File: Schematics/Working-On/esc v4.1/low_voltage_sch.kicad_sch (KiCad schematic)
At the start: 28 parts, among them IC1 74HCT08BQ,115, IC2 74HCT08BQ,115, U2 ATmega328P-M

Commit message: New connectors, and BEMF Filter.
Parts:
- removed C12: 8200pF, Capacitor_SMD:C_0402_1005Metric, symbol Device:C
- added C24: 2.5n, Capacitor_SMD:C_0402_1005Metric, symbol Device:C
- added R23, R24, R5: 10k, Resistor_SMD:R_0402_1005Metric, symbol Device:R
- 8MHz1: value ECS-80-12-30BQ-JES-TR -> ECS-80-12-33-JGN-TR; footprint ECS-80-12-30BQ-JES-TR:ECS-80-12_ECS -> Crystal:Crystal_SMD_3225-4Pin_3.2x2.5mm
- C11, C7: value 8200pF -> 2.5n
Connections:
- net COIL_A_BEMF: now also C7.2, R5.2; no longer C7.1, R3.1, R4.2
- net COIL_B_BEMF: now also C11.2, R23.2; no longer C11.1, R6.1, R7.2
- net COIL_C_BEMF: now also C24.2, R24.2; no longer R19.1, R20.2
- net GND: now also C11.1, C7.1, C24.1; no longer C11.2, C7.2
- net PWM: now reaches U2.1 (PD3)
- new net: R19.1, R20.2, R24.1
- new net: R23.1, R6.1, R7.2
- new net: R3.1, R4.2, R5.1
- no-connect marks 11 -> 10
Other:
- moved on the sheet: C11, C13, C19, C7, IC1, IC2, R19, R20, R3, R4, R6, R7

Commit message: VIA update
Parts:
- removed R9: 1k, Resistor_SMD:R_0402_1005Metric, symbol Device:R
- added C12: 47uF, Capacitor_SMD:C_0805_2012Metric, symbol Device:C
- added L2: 100uH, Inductor_SMD:L_0805_2012Metric, symbol Device:L
- C11, C24, C7: value 2.5n -> 2.4n
- C23: value 10uF -> 47uF; footprint Capacitor_SMD:C_0603_1608Metric -> Capacitor_SMD:C_0805_2012Metric
- L1: value 2.2mH -> 100uH; footprint 744045222:WE-LQ_L49 -> Inductor_SMD:L_0805_2012Metric
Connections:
- net COMP_REF_IN: now also C12.2, L2.2; no longer C23.2, L1.2
- net GND: now also C12.1
- new net: C23.2, L1.2, L2.1
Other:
- note removed: "fc = 1 kHz"
- moved on the sheet: C23, L1, R1, R8

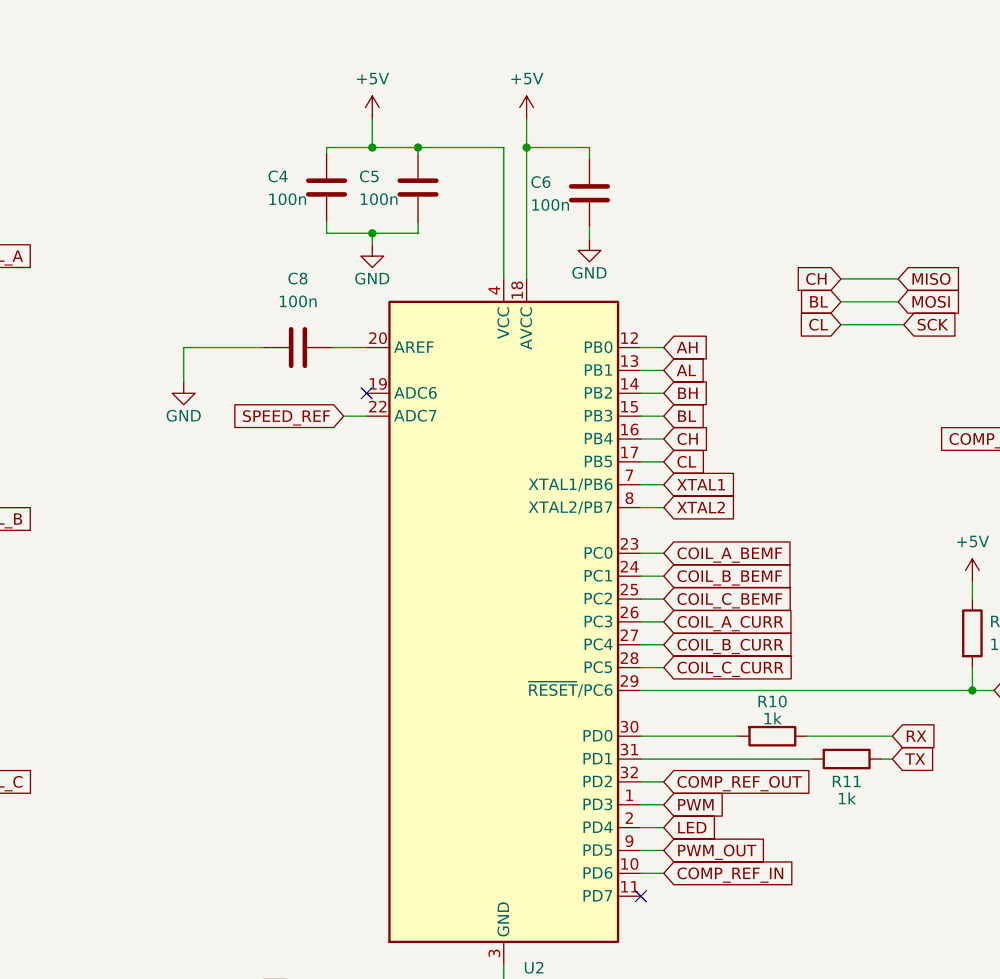
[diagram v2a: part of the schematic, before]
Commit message: swaped PWM_IN & Comp_Ref_Out, vias finished
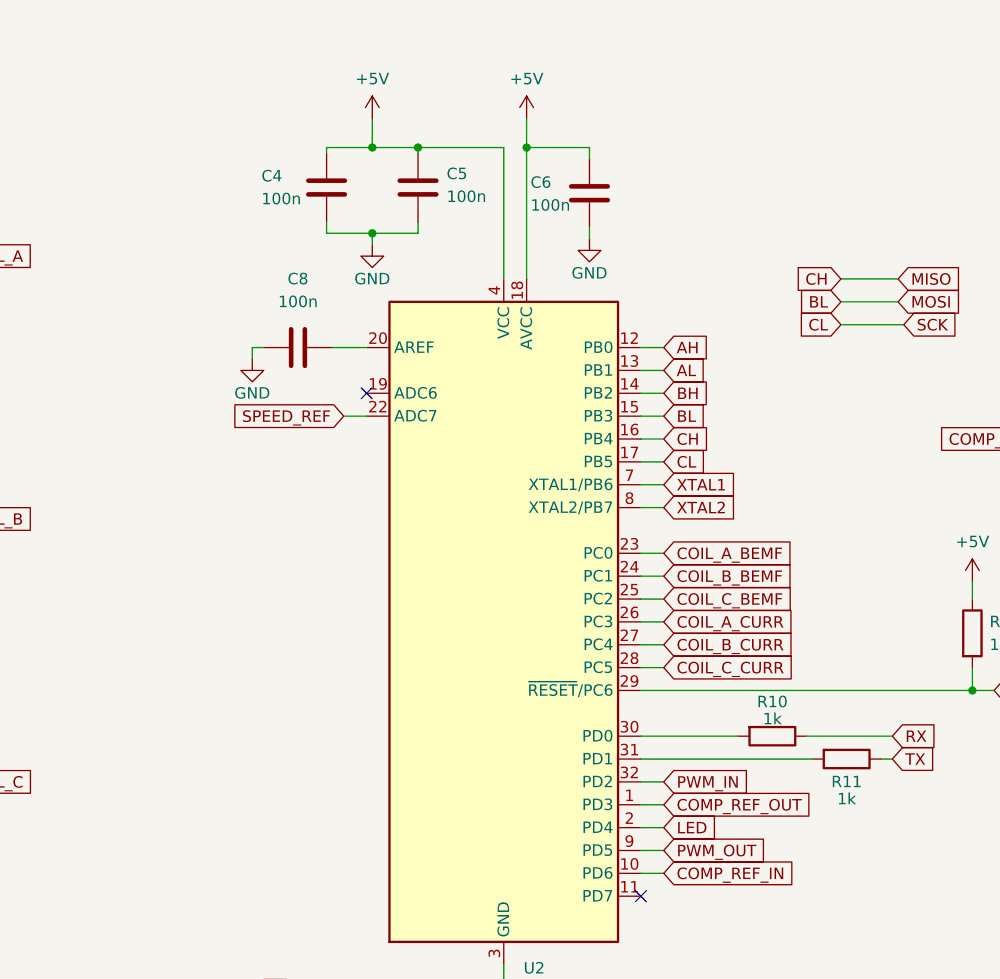
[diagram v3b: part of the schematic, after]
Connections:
- net PWM is gone; now on net COMP_REF_OUT: U2.1 (PD3)
- net COMP_REF_OUT: no longer U2.32 (PD2)
- new net PWM_IN: U2.32 (PD2)
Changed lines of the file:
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@@
 	(wire
 		(pts
-			(xy 120.65 71.12) (xy 120.65 74.93)
+			(xy 128.27 71.12) (xy 128.27 72.39)
 		)
 		(stroke
@@
 	(wire
 		(pts
-			(xy 129.54 71.12) (xy 120.65 71.12)
+			(xy 128.27 71.12) (xy 129.54 71.12)
 		)
 		(stroke
@@
 		)
 	)
-	(global_label "PWM"
+	(global_label "PWM_IN"
 		(shape input)
-		(at 173.99 121.92 0)
+		(at 173.99 119.38 0)
 		(fields_autoplaced yes)
 		(effects
@@
 		)
 		(property "Intersheetrefs" "${INTERSHEET_REFS}"
-			(at 181.148 121.92 0)
+			(at 184.0509 119.38 0)
 			(effects
 				(font
@@
 	(global_label "COMP_REF_OUT"
 		(shape input)
-		(at 173.99 119.38 0)
+		(at 173.99 121.92 0)
 		(fields_autoplaced yes)
 		(effects
@@
 		)
 		(property "Intersheetrefs" "${INTERSHEET_REFS}"
-			(at 191.3685 119.38 0)
+			(at 191.3685 121.92 0)
 			(effects
 				(font
@@
 		(dnp no)
 		(property "Reference" "C5"
-			(at 140.1318 52.1462 0)
+			(at 149.86 51.816 0)
 			(effects
 				(font
@@
 		)
 		(property "Value" "100n"
-			(at 140.1318 54.6862 0)
+			(at 149.86 54.356 0)
 			(effects
 				(font
@@
 		(dnp no)
 		(property "Reference" "C4"
-			(at 129.9718 52.1462 0)
+			(at 129.286 52.07 0)
 			(effects
 				(font
@@
 		)
 		(property "Value" "100n"
-			(at 129.9718 54.6862 0)
+			(at 129.286 54.61 0)
 			(effects
 				(font
@@
 	(symbol
 		(lib_id "power:GND")
-		(at 120.65 74.93 0)
+		(at 128.27 72.39 0)
 		(unit 1)
 		(exclude_from_sim no)
@@
 		(dnp no)
 		(property "Reference" "#PWR019"
-			(at 120.65 81.28 0)
+			(at 128.27 78.74 0)
 			(effects
 				(font
@@
 		)
 		(property "Value" "GND"
-			(at 120.65 78.74 0)
+			(at 128.27 76.2 0)
 			(effects
 				(font
@@
 		)
 		(property "Footprint" ""
-			(at 120.65 74.93 0)
+			(at 128.27 72.39 0)
 			(effects
 				(font
@@
 		)
 		(property "Datasheet" ""
-			(at 120.65 74.93 0)
+			(at 128.27 72.39 0)
 			(effects
 				(font
@@
 		)
 		(property "Description" ""
-			(at 120.65 74.93 0)
+			(at 128.27 72.39 0)
 			(effects
 				(font

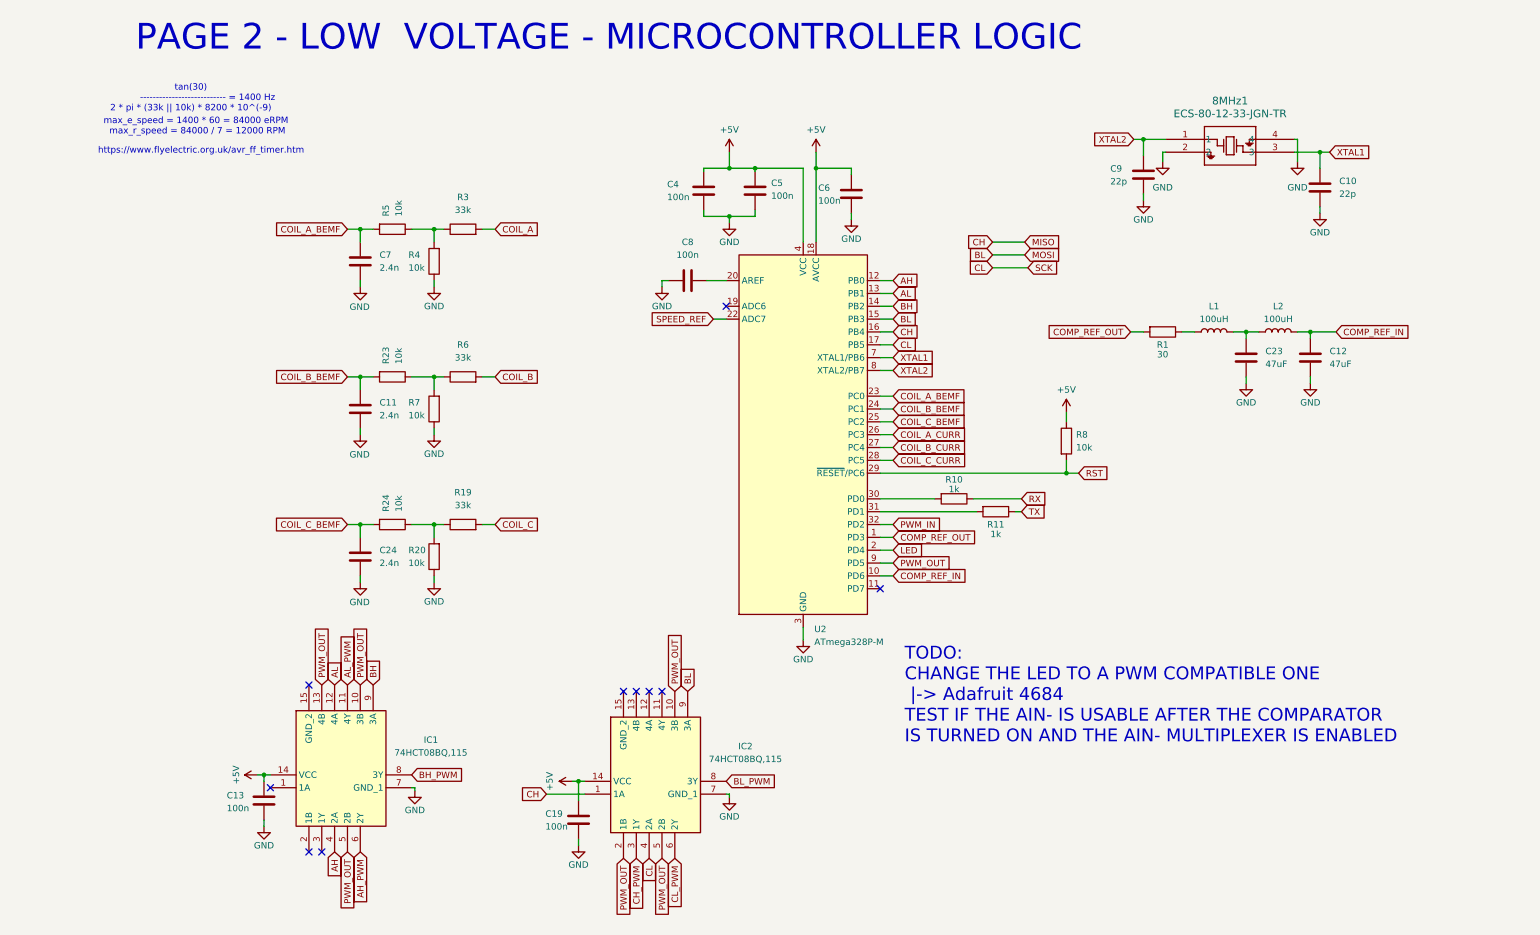
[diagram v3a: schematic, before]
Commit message: Added pins for the BACK-EMFs and PWM Control signals
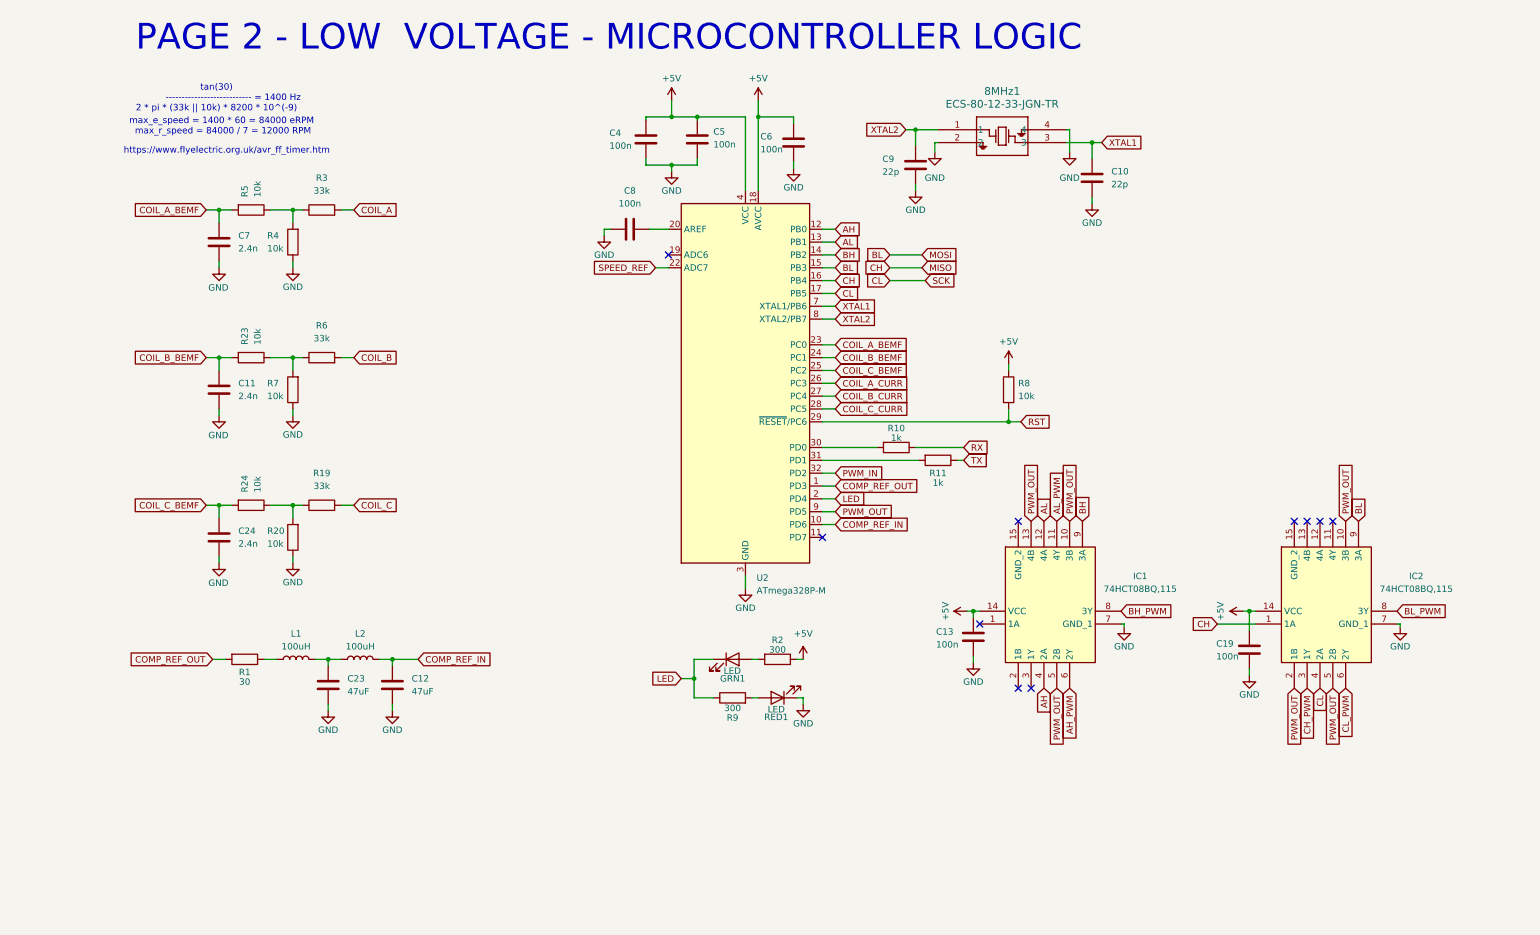
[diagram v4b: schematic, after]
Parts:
- added GRN1, RED1: LED, LED_SMD:LED_0603_1608Metric, symbol Device:LED
- added R2, R9: 300, Resistor_SMD:R_0402_1005Metric, symbol Device:R
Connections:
- net +5V: now also R2.1
- net GND: now also RED1.1 (K)
- net LED: now also GRN1.1 (K), R9.1
- new net: R9.2, RED1.2 (A)
- new net: GRN1.2 (A), R2.2
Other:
- note removed: "TODO: CHANGE THE LED TO A PWM COMPATIBLE ONE |-> Adafruit 4684 TEST IF THE AIN- IS USABLE AFTER THE COMPARATOR IS TURNED ON AND THE AIN- MULTIPLEXER IS ENABLED"
- moved on the sheet: 8MHz1, C10, C11, C12, C13, C19, C23, C24, C4, C5, C6, C7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
